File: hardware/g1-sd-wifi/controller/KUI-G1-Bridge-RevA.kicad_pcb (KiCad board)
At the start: 4 copper layers, 59 x 105 mm, 364 parts, among them J10 FPGA JTAG pogo pads, J20 5V/GND direct wire pads, J201 microSD push-pull 1.42mm, J202 RP USB service pads, J203 RP SWD/reset/boot pads, J204 C5 direct UART recovery pads, J40 FH12-14S-0.5SH(55), J41 FH12-6S-0.5SH(55), J50 FH12-20S-0.5SH(55), J51 FH12-20S-0.5SH(55), K201 C5 removable compression cont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, K202 C5 removable compression cont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, K203 C5 removable compression cont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, K204 C5 removable compression cont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, K205 C5 removable compression cont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, K206 C5 removable compression cont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, K207 C5 removable compression cont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, K208 C5 removable compression cont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, K209 C5 removable compression cont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, K210 C5 removable compression cont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, K211 C5 removable compression cont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, K212 C5 removable compression cont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, K213 C5 removable compression cont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, K214 C5 removable compression cont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, K215 C5 removable compression cont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, K216 C5 removable compression cont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, Q20 PMV48XP reverse polarity, Q201 C5 recovery pull-down, Q202 C5 recovery pull-down, U10 LCMXO2-2000HC-4TG100C, U20 TPS2116 automatic mux, U201 RP2350B, U202 16MiB boot NOR, U203 8MiB QSPI PSRAM, U204 C5 off-state isolation, U205 C5 off-state isolation, U207 SD4-bit DAT rail isolation, U208 SD CLK/CMD rail isolation, U209 SD enable/power-good NAND, U21 TPS62162 3.3V 1A, U22 TPS62162 3.3V 1A, U23 TPS3808G33DBVR, U24 TPS3808G33DBVR, U25 TPS3808G33DBVR, U26 TPS3808G01DBVR, U27 SN74LVC2G08DCUR, U28 SN74LVC2G08DCUR, U29 SN74LVC2G08DCUR, U30 SN74LVC1G11DBVR, U31 SN74LVC2G04DBVT, U32 SN74LVC1G32DBVR, U33 SN74LVC1G08DBVR, U34 SN74LVC1G08DBVR, U35 SN74LVC16T245, U36 SN74LVC244A host controls, U37 SN74LVC1G17 host RESETn, U38 SN74LVC1G125 qualified ATA_IN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, U39 SN74LVC1G125 qualified ATA_DM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, U40 MX29LV640ETTI-70G x8 / 4 x 2M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, U41 SN74LVC2G125 bank-domain buff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, U42 SN74LVC1G11 write-authorize A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, U43 SN74LVC1G04 write-block inver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, U44 SN74LVC1G332 NOR WE qualifier, U45 TLV803EB29 console-rail NOR r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, U70 SN74LVC1G07 open-drain IORDY, U71 TPS22919 Wi-Fi input switch, U72 SN74LVC1G32DBVR, U73 SN74LVC1G32DBVR, X10 50MHz 3.3V, X201 12MHz

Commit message: G1 carrier: 1k R410, 4.18 V loss threshold, local bypass placement
- R410 becomes a 1 kOhm pull-up (reused 0402 part), so a selector harness
  fitted with R410 still present cannot short console 3.3 V.
- R270 (4.7 kOhm, reused part) lowers the U26 loss threshold from 4.358 V
  to 4.180 V; the divider now sits beside U26 instead of 27 mm away.
- 28 owner-assigned bypass capacitors placed next to their ICs with a new
  placer (tools/place_local_bypass.py); C230 and the DNP BIOS caps for
  U42/U43 remain open. C236 moves to the C5 load.
- tools/update_board_from_netlist.py applies reviewed schematic changes to
  the routed board without re-placing it.
- generate_design.py takes KICAD10_FOOTPRINT_DIR so an older system library
  cannot overwrite the localized KiCad 10 footprints.

Native ERC 0, DRC 0, parity 0; integration audit refreshed and passing.

Co-Authored-By: Claude Opus 5.5 <noreply@anthropic.com>
Claude-Session: https://claude.ai/code/session_01Gp9EYc2r9fMpZ7V8WtfonZ
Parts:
- added R270: 4.7k, KUI_Footprints:R_0402_1005Metric, F.Cu at (91.7, 69.4)
- R410: value 0R -> 1k; footprint KUI_Footprints:R_0603_1608Metric -> KUI_Footprints:R_0402_1005Metric
- moved C236 78.7 mm to (96.0, 53.1), turned to 90 degrees
- moved C2036 44.9 mm to (82.7, 65.2), turned to 180 degrees
- moved C221 33.6 mm to (85.7, 65.1)
- moved C215 32.0 mm to (86.5, 69.0), turned to -90 degrees
- moved C232 29.9 mm to (71.3, 67.5), turned to 180 degrees
- moved C234 28.4 mm to (81.3, 116.1), turned to 180 degrees
- moved C401 28.3 mm to (103.2, 131.5), turned to 0 degrees
- moved R210 27.7 mm to (93.6, 69.1), turned to -90 degrees
- moved C400 26.0 mm to (95.4, 143.3), turned to 180 degrees
- moved C222 25.4 mm to (79.2, 94.5), turned to 180 degrees
- moved C219 24.7 mm to (72.3, 80.1)
- moved C119 24.0 mm to (79.8, 65.7), turned to 90 degrees
- moved C223 23.9 mm to (96.7, 50.1), turned to 90 degrees
- moved C233 23.1 mm to (71.2, 91.9), turned to -90 degrees
- moved C229 22.2 mm to (112.8, 109.4), turned to 90 degrees
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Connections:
- R210 pad 2: GND -> PRIMARY_SENSE_LO
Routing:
- net GND: track 222.8 -> 199.6 mm, vias 278 -> 247

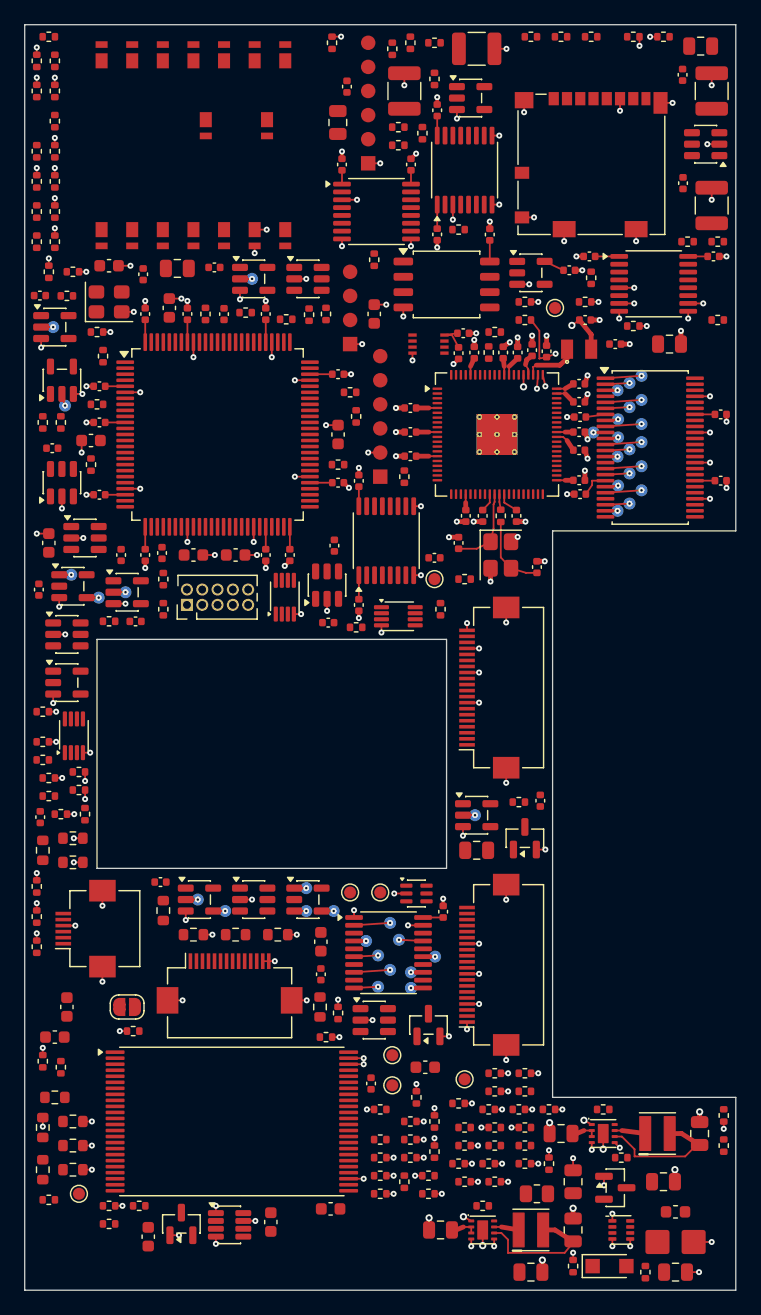
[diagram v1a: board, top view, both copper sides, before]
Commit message: G1 carrier: connectivity-driven passive placement, In2 3V3 plane, router fix
- Re-place 69 signal passives next to the pins they serve
  (tools/replace_passives.py); the original packer left series and pull
  resistors up to 70 mm from both partners, including USB, SD and FPGA
  clock series resistors. ICs, connectors, probes and locked reviewed
  routes stay fixed.
- Move the 32 data-line pull-downs to U35/U10/J50/J51 where space allows.
- In2.Cu becomes the +3V3_LOGIC plane (tools/add_power_plane.py).
- export-dsn strips the In1 wire_keepout, which Freerouting 1.9 treated as
  a via obstacle, so earlier runs could only route on F.Cu.
- EDA-ENVIRONMENT.md records the KiCad 10 source build and these findings.
- docs/OWNER-NEXT-STEPS.md lists what still needs the owner.

Native DRC 0 violations, parity 0; routing not yet closed.

Co-Authored-By: Claude Opus 5.5 <noreply@anthropic.com>
Claude-Session: https://claude.ai/code/session_01Gp9EYc2r9fMpZ7V8WtfonZ
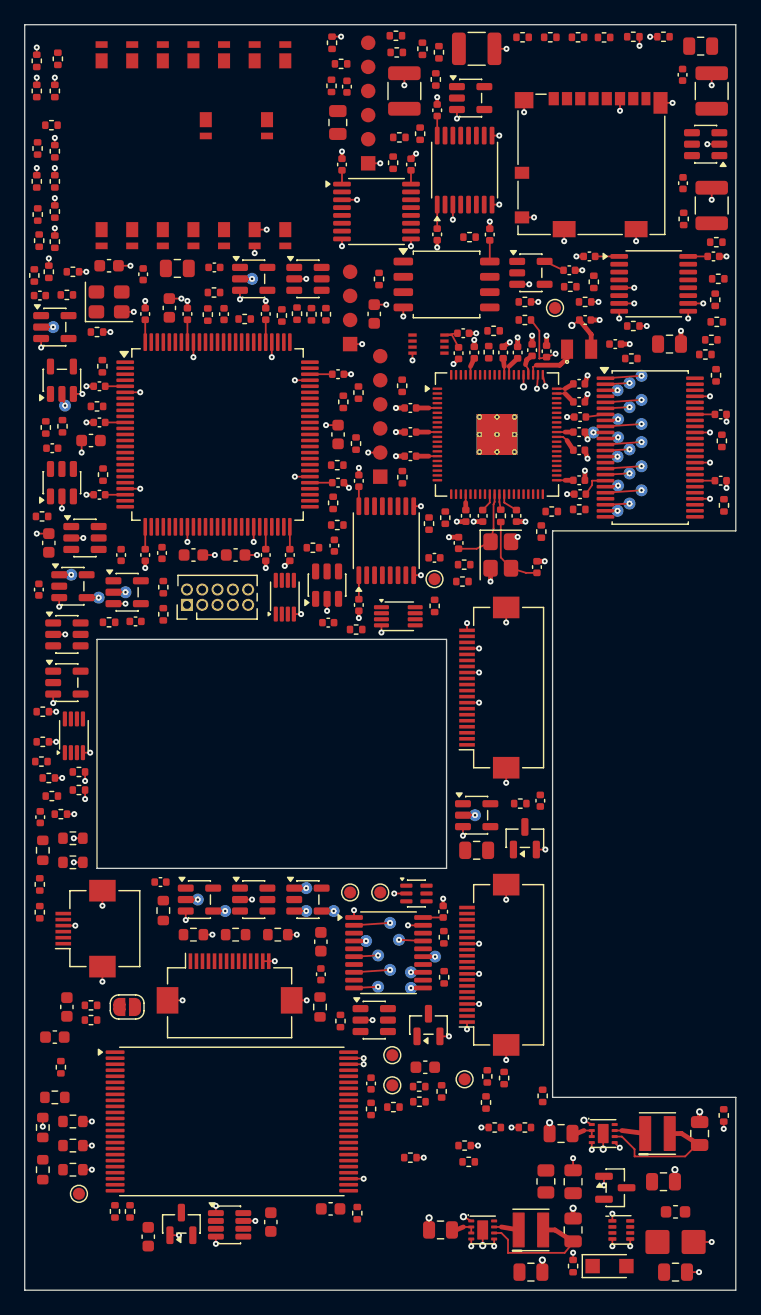
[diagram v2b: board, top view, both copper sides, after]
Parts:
- moved R266 96.8 mm to (72.8, 47.8), turned to -90 degrees
- moved R234 94.8 mm to (124.7, 61.1), turned to 90 degrees
- moved R253 88.6 mm to (72.2, 53.3), turned to 180 degrees
- moved R247 77.4 mm to (85.7, 67.2), turned to 180 degrees
- moved R240 76.2 mm to (115.3, 66.7), turned to 180 degrees
- moved R231 74.4 mm to (127.3, 67.8)
- moved R233 74.4 mm to (127.5, 66.1), turned to 0 degrees
- moved R224 73.5 mm to (126.5, 72.4), turned to 0 degrees
- moved R225 72.0 mm to (127.0, 71.1), turned to 0 degrees
- moved R249 71.3 mm to (117.2, 66.3), turned to 90 degrees
- moved R227 69.2 mm to (127.8, 79.5), turned to -90 degrees
- moved R229 67.8 mm to (128.0, 84.9), turned to -90 degrees
- moved R270 67.1 mm to (108.3, 134.4), turned to 90 degrees
- moved R223 63.7 mm to (127.4, 74.1), turned to 90 degrees
- moved R205 63.0 mm to (103.0, 47.0), turned to -90 degrees
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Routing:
- net GND: track 199.6 -> 180.4 mm, vias 247 -> 215
- added copper zone on In2.Cu, net +3V3_LOGIC

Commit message: G1 carrier: re-floorplan around the FPGA on six layers (unrouted)
The four-layer placement stalled the router at 300+ open connections.
Pin plan and floorplan were the cause, not just layer count:

- FPGA pins follow the placement (design/fpga-pin-swap-2026-10-10.json):
  the RP2350 link bus moves to the east edge facing the controller (it
  was on the west edge, wrapping round the chip), BUS_DD to the south
  edge in U35's A-side order, host controls/requests/BIOS lines to the
  west edge, the 50 MHz clock to PCLKT5_0 (pin 3). Only FPGA_CLK50 is a
  clock in the RTL; all other moves are plain LVCMOS33 I/O. LPF and pin
  table regenerate from frontend.json via tools/sync_fpga_pins.py.
- U35 turns +90 degrees and sits directly under the FPGA (which moves
  2.26 mm north), so the data bus drops straight between them.
- The 16 raw ATA_DD probes and their ground probe move from U35 (whose
  B side now faces the BIOS aperture) to U40's pins on the same nets.
- Small ICs, bypass capacitors and passives are re-placed by
  connectivity; narrow plane fanout regenerated; six-layer stack
  (F / GND / sig / sig / +3V3 / B, 0.8 mm).

tools/floorplan_2026_10_10.sh reproduces the board from the previous
commit. ERC 0, schematic parity 0, native DRC 0 violations; integration
audit and FPGA checks pass. Routing is in progress.

Co-Authored-By: Claude Opus 5.5 <noreply@anthropic.com>
Claude-Session: https://claude.ai/code/session_01Gp9EYc2r9fMpZ7V8WtfonZ
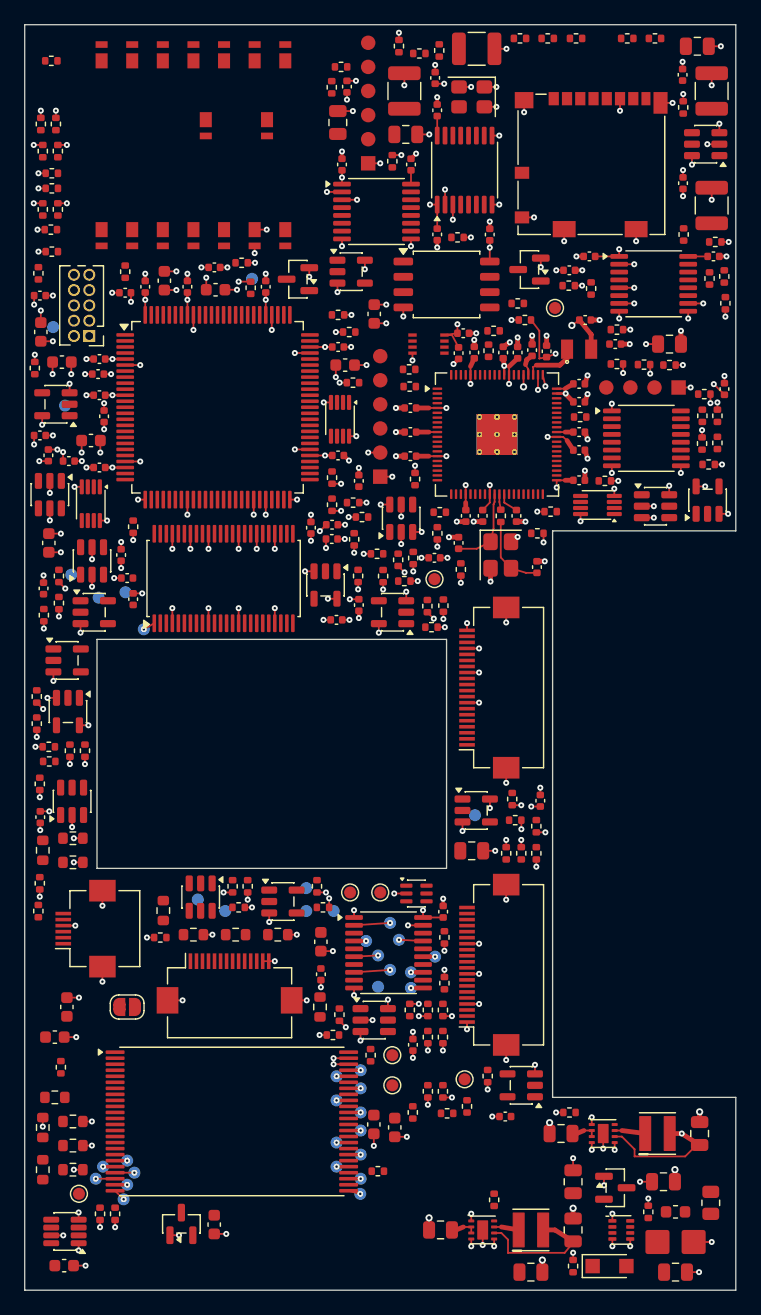
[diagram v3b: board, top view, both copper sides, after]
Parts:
- moved R265 78.7 mm to (95.5, 50.2), turned to -90 degrees
- moved TP110 74.5 mm to (78.2, 142.5)
- moved TP111 72.3 mm to (78.5, 141.2)
- moved TP112 72.0 mm to (75.9, 140.8)
- moved TP113 70.5 mm to (79.1, 140.2)
- moved TP114 70.3 mm to (76.5, 139.8)
- moved R234 69.5 mm to (102.0, 126.8)
- moved TP100 69.4 mm to (95.9, 139.8)
- moved R231 68.9 mm to (71.2, 108.0), turned to -90 degrees
- moved TP115 67.5 mm to (78.5, 139.2)
- moved TP101 66.9 mm to (97.9, 138.8)
- moved TP102 66.6 mm to (95.9, 137.8)
- moved R249 65.2 mm to (81.2, 120.7), turned to 180 degrees
- moved TP136 64.9 mm to (97.9, 140.8)
- moved TP109 64.8 mm to (97.8, 142.0)
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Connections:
- U10 pad 1: LINK_D0 -> REQ_DMARQ_OEn
- U10 pad 10: LINK_D6 -> BUS_DA2
- U10 pad 12: LINK_D7 -> BUS_CS0n
- U10 pad 13: LINK_WRn -> BUS_CS1n
- U10 pad 14: LINK_RDn -> BUS_DIORn
- U10 pad 15: LINK_A0 -> BUS_DIOWn
- U10 pad 16: LINK_A1 -> BUS_DMACKn
- U10 pad 17: LINK_IRQ -> BUS_RESETn
- U10 pad 18: LINK_READY -> REQ_INTRQ
- U10 pad 19: FPGA_RESETn -> BIOS_RECOVERYn
- U10 pad 2: LINK_D1 -> REQ_INTRQ_OEn
- U10 pad 20: FPGA_CLK50 -> BIOS_WR_EN
- U10 pad 21: BRIDGE_ARM -> REQ_DMARQ
- U10 pad 24: BUS_SAFE -> REQ_IORDY_LOW
- U10 pad 25: PWR_FAILn -> BUS_SAFE
- U10 pad 28: BUS_DA0 -> BUS_DD0
- U10 pad 29: BUS_DA1 -> BUS_DD1
- U10 pad 3: unconnected-(U10-PL3A-Pad3) -> FPGA_CLK50
- U10 pad 30: BUS_DA2 -> BUS_DD2
- U10 pad 34: BUS_CS0n -> BUS_DD3
- U10 pad 35: BUS_CS1n -> BUS_DD4
- U10 pad 36: BUS_DIORn -> BUS_DD5
- U10 pad 37: BUS_DIOWn -> BUS_DD6
- U10 pad 38: BUS_RESETn -> BUS_DD7
- U10 pad 39: BUS_DMACKn -> BUS_DD8
- U10 pad 4: LINK_D2 -> BIOS_BANK1
- U10 pad 40: REQ_INTRQ_OEn -> BUS_DD9
- U10 pad 41: REQ_DMARQ_OEn -> BUS_DD10
- U10 pad 42: unconnected-(U10-PB21A-Pad42) -> BUS_DD11
- U10 pad 43: unconnected-(U10-PB21B-Pad43) -> BUS_DD12
- U10 pad 45: unconnected-(U10-PB22A-Pad45) -> BUS_DD13
- U10 pad 47: unconnected-(U10-PB22B-Pad47) -> BUS_DD14
- U10 pad 51: BUS_DD0 -> BUS_DD15
- U10 pad 52: BUS_DD1 -> FPGA_READY
- U10 pad 53: BUS_DD2 -> REQ_DATA_OEn
- U10 pad 54: BUS_DD3 -> DATA_DIR
- U10 pad 57: BUS_DD4 -> PWR_FAILn
- U10 pad 58: BUS_DD5 -> BRIDGE_ARM
- U10 pad 59: BUS_DD6 -> FPGA_RESETn
- U10 pad 60: BUS_DD7 -> LINK_READY
- U10 pad 61: BUS_DD8 -> LINK_IRQ
- U10 pad 62: BUS_DD9 -> LINK_A1
- U10 pad 63: BUS_DD10 -> LINK_A0
- U10 pad 64: BUS_DD11 -> LINK_RDn
- U10 pad 65: BUS_DD12 -> LINK_WRn
- U10 pad 66: BUS_DD13 -> LINK_D7
- U10 pad 67: BUS_DD14 -> LINK_D6
- U10 pad 68: BUS_DD15 -> LINK_D5
- U10 pad 69: REQ_DATA_OEn -> LINK_D4
- U10 pad 7: LINK_D3 -> BIOS_BANK0
- U10 pad 70: DATA_DIR -> LINK_D3
- U10 pad 71: REQ_IORDY_LOW -> LINK_D2
- U10 pad 74: REQ_INTRQ -> LINK_D1
- U10 pad 75: REQ_DMARQ -> LINK_D0
- U10 pad 78: BIOS_BANK0 -> unconnected-(U10-PT22A-Pad78)
- U10 pad 8: LINK_D4 -> BUS_DA0
- U10 pad 83: BIOS_BANK1 -> unconnected-(U10-PT19B-Pad83)
- U10 pad 84: BIOS_WR_EN -> unconnected-(U10-PT19A-Pad84)
- U10 pad 9: LINK_D5 -> BUS_DA1
- U10 pad 96: BIOS_RECOVERYn -> unconnected-(U10-PT11B-Pad96)
- U10 pad 97: FPGA_READY -> unconnected-(U10-PT11A-Pad97)
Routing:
- net +3V3_LOGIC: track 68.8 -> 146.8 mm, vias 0 -> 121
- net GND: track 180.4 -> 227.0 mm, vias 215 -> 281
- net CONSOLE_3V3: track 4.03 -> 0.00 mm
- net ATA_DD10: track 3.00 -> 1.00 mm
- net ATA_DD7: track 3.00 -> 1.00 mm
- net ATA_DD5: track 3.00 -> 1.00 mm
- net ATA_DD2: track 3.00 -> 1.00 mm
- net DATA_DIR: track 3.00 -> 1.00 mm
- net +3V3_STORAGE: track 14.4 -> 12.8 mm
- net ATA_DD13: track 3.00 -> 1.60 mm
- net REQ_IORDY_LOW: track 1.00 -> 0.00 mm, vias 1 -> 0
- net REQ_DMARQ_OEn: track 1.00 -> 0.00 mm, vias 1 -> 0
- net REQ_DATA_OEn: track 1.00 -> 0.00 mm, vias 1 -> 0
- net IORDY_RELEASE: track 1.00 -> 0.00 mm, vias 1 -> 0
- net INTRQ_OEn: track 1.00 -> 0.00 mm, vias 1 -> 0
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- added copper zone on In4.Cu, net +3V3_LOGIC
- removed copper zone on In2.Cu, net +3V3_LOGIC
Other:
- copper layers 4 -> 6

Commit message: G1 carrier: IC fanout drops vias under the body; dangling-copper cleanup
- add_carrier_ground_fanout: pins of parts with more than eight pads try
  the inward direction first, so plane vias land under the IC body. The
  FPGA's south power/ground vias had landed in the 1.4 mm gap the data
  bus must cross to U35.
- floorplan_2026_10_10.sh starts from the four-layer placement (BASE,
  default 4c525f6); board regenerated: 165/165 parts placed, native DRC
  0 violations, schematic parity 0.
- remove_dangling_copper.py: delete the unlocked vias and stubs that
  native DRC reports dangling after a router session, repeating until
  none remain; locked copper is only reported.
- OWNER-NEXT-STEPS: confirm a six-layer 0.8 mm stack with the fabricator.

Co-Authored-By: Claude Opus 5.5 <noreply@anthropic.com>
Claude-Session: https://claude.ai/code/session_01Gp9EYc2r9fMpZ7V8WtfonZ
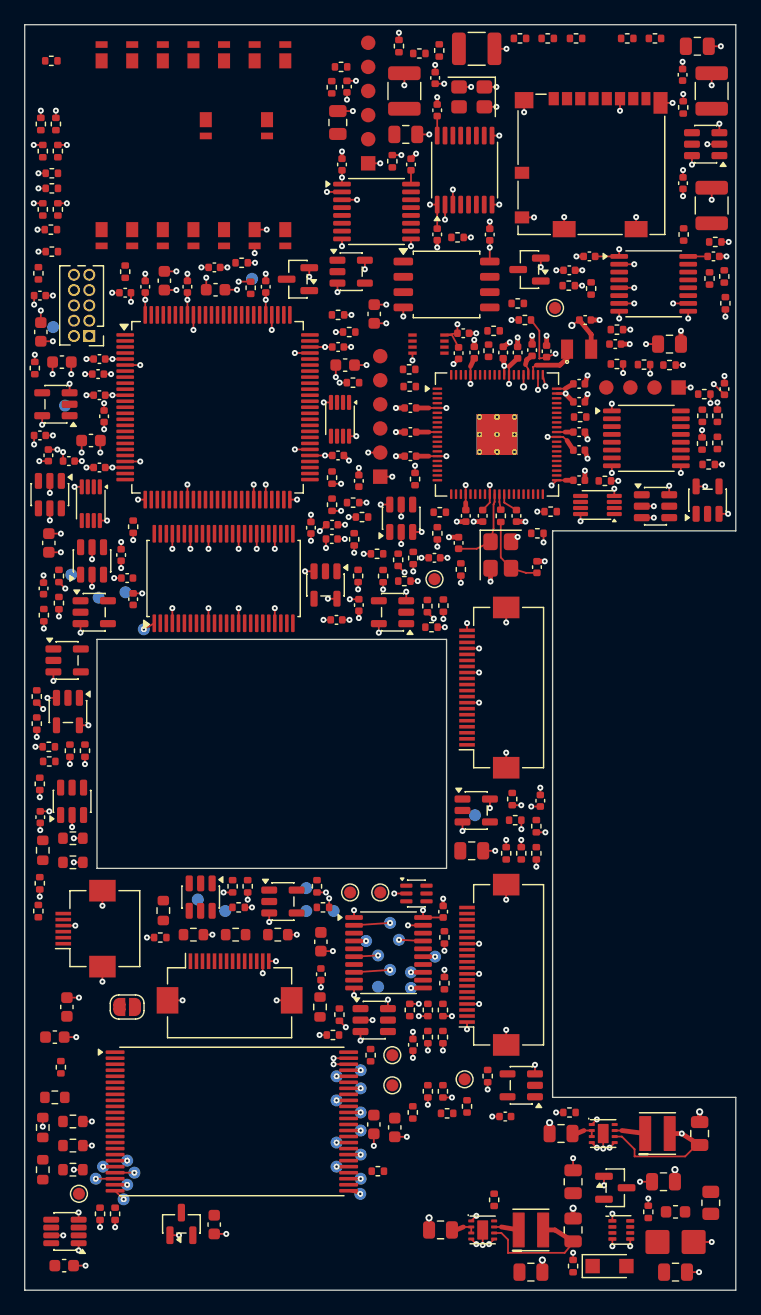
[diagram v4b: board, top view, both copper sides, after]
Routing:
- net GND: track 227.0 -> 227.6 mm, vias 281 -> 282
